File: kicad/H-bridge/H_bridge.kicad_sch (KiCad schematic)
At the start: 34 parts, among them J1 Screw_Terminal_01x02, J2 Conn_Coaxial, J3 Loop_terminals, J4 Coil_terminals, Q1 IAUT300N10S5N014ATMA1, Q2 IAUT300N10S5N014ATMA1, Q3 IAUT300N10S5N014ATMA1, Q4 IAUT300N10S5N014ATMA1, U1 LTV-817, U2 PDS1-S15-S15-M, U3 HIP4080A

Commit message: First iteration of the layout
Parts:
- removed C8: C, symbol Device:C
- removed J3: Loop_terminals, symbol Connector:Screw_Terminal_01x02
- removed J4: Coil_terminals, symbol Connector:Screw_Terminal_01x02
- removed R7: R_US, symbol Device:R_US
- added J3: 2453710000, footprints:CONN_2453710000, symbol Connector:Screw_Terminal_01x04
- added RV1: V20E50P (80V), Varistor:RV_Disc_D15.5mm_W7.5mm_P7.5mm, symbol Device:Varistor_US
- C1, C2, C5, C6: footprint Capacitors_SMD:C_0805 -> Capacitor_SMD:C_0805_2012Metric
- C3, C4, C7, C9: footprint (none) -> Capacitor_SMD:C_0805_2012Metric
- D1, D2: value D -> PMEG10020AELRX; footprint (none) -> Diode_SMD:Nexperia_CFP3_SOD-123W; DIGIKEY (none) -> 1727-2283-1-ND; PARTNO (none) -> PMEG10020AELRX
- Q1, Q2, Q3, Q4: footprint (none) -> Package_TO_SOT_SMD:Infineon_PG-HSOF-8-1_ThermalVias
- R2: footprint Resistors_SMD:R_0805 -> Resistor_SMD:R_0805_2012Metric
- R3, R4, R5, R6: footprint (none) -> Resistor_SMD:R_0805_2012Metric
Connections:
- net GNDD: now also J3.4 (Pin_4), RV1.2
- net at R2.1, U1.3: now also U3.6 (IN+)
- net Coil_B: now reaches C3.2, Q3.3 (S), Q4.1 (D), U3.12 (AHS)
- net Coil_B: now also J3.3 (Pin_3)
- net Coil_A: now reaches C7.2, Q1.3 (S), Q2.1 (D), U3.19 (BHS)
- net Coil_A: now also J3.2 (Pin_2)
- net Current_in: now reaches Q1.1 (D), Q3.1 (D)
- net Current_in: now also J3.1 (Pin_1), RV1.1
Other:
- moved on the sheet: R2

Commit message: 2nd iteration
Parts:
- added H1, H2, H3, H4: MountingHole, MountingHole:MountingHole_3.5mm, symbol Mechanical:MountingHole
- Q1, Q2, Q3, Q4: symbol Simulation_SPICE:NMOS -> Device:Q_NMOS_GDS
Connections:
- net Coil_A: now also Q2.2 (D); no longer Q2.1 (D)
- net Coil_B: now also Q4.2 (D); no longer Q4.1 (D)
- net Current_in: now also Q1.2 (D), Q3.2 (D); no longer Q1.1 (D), Q3.1 (D)
- net at U3.13 (ALO): now also Q4.1 (G); no longer Q4.2 (G)
- net at U3.11 (AHO): now also Q3.1 (G); no longer Q3.2 (G)
- net at U3.20 (BHO): now also Q1.1 (G); no longer Q1.2 (G)
- net at U3.18 (BLO): now also Q2.1 (G); no longer Q2.2 (G)

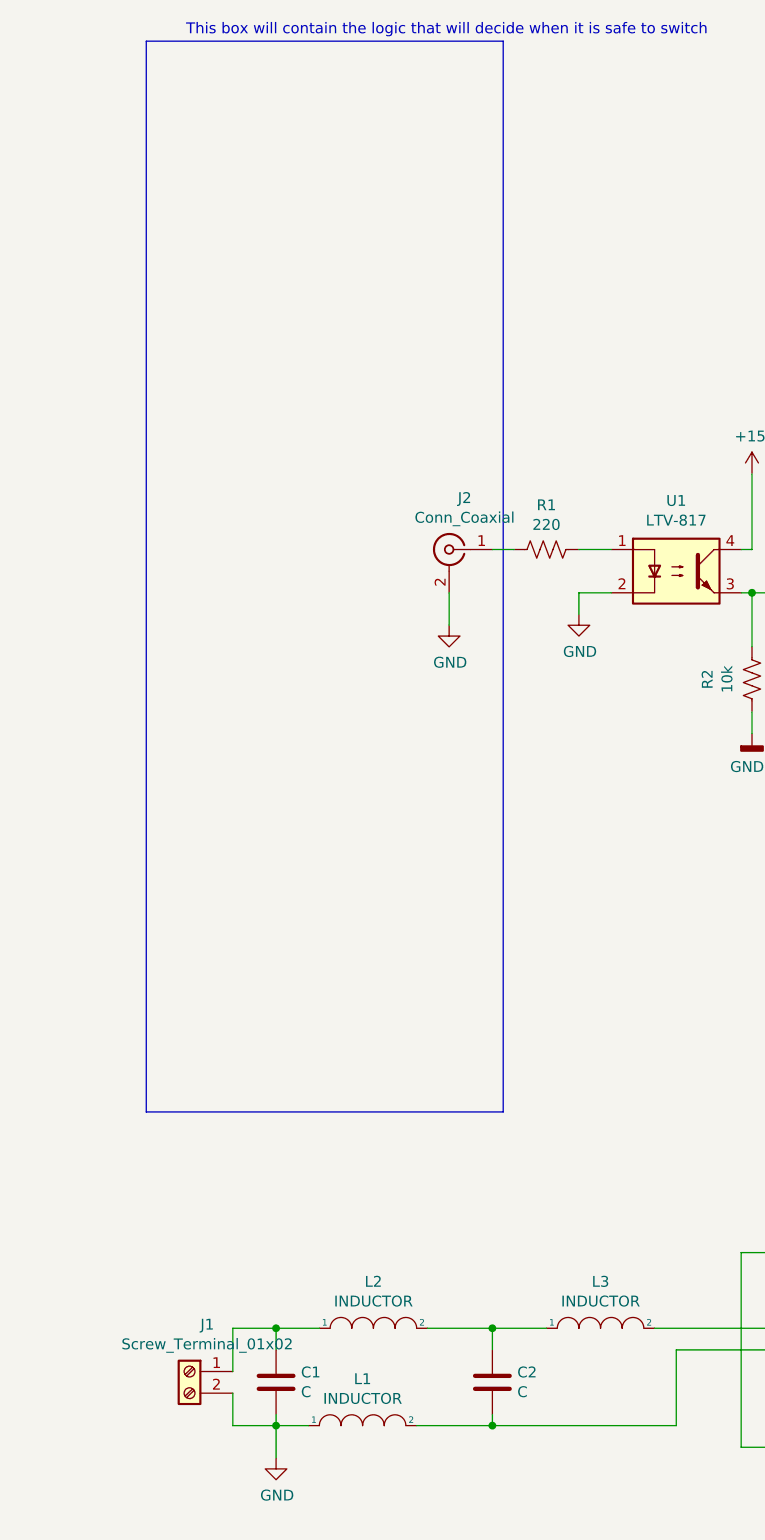
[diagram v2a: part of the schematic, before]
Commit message: H_bridge circuit with current control ciruit added
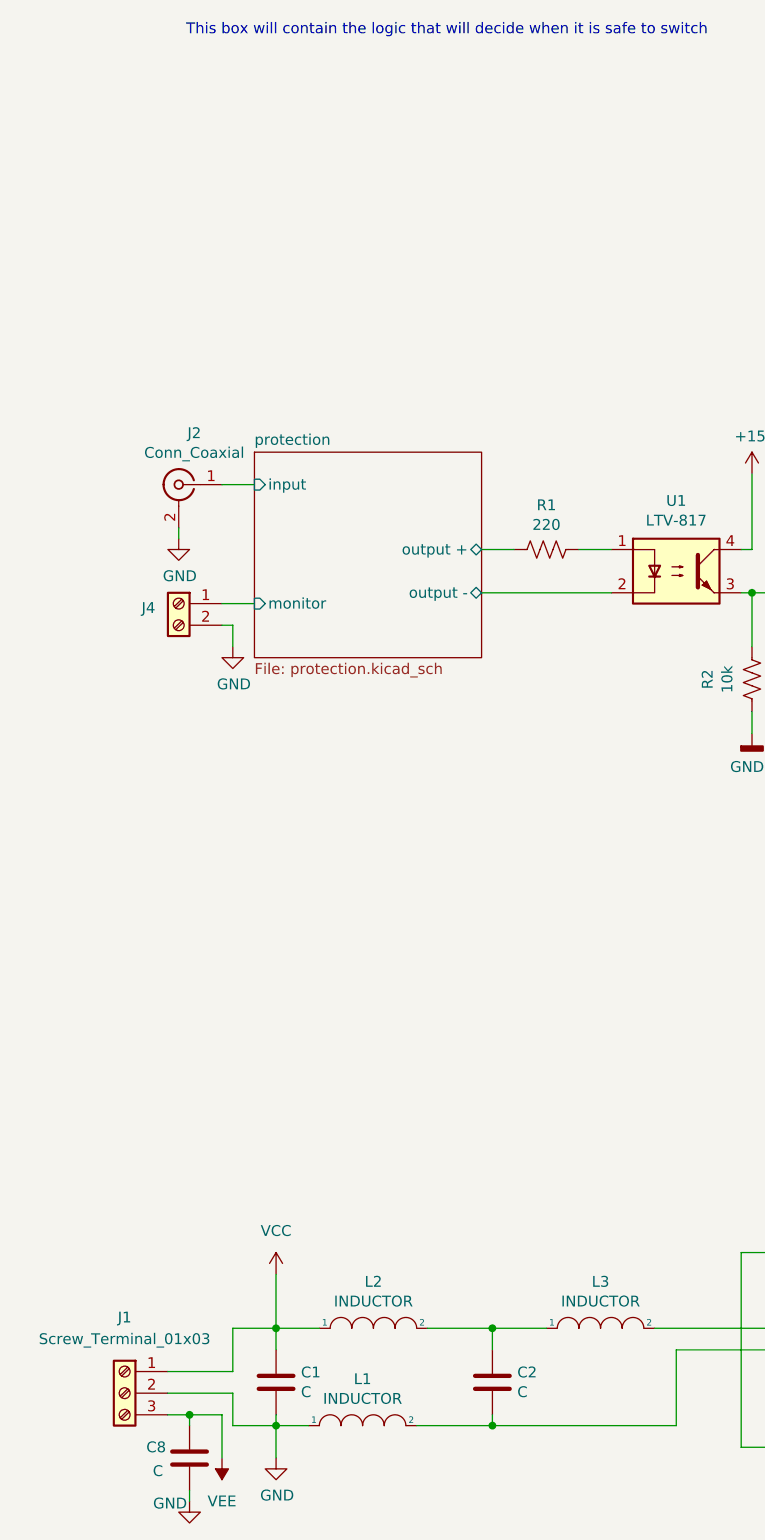
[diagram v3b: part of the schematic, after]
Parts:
- removed J1: Screw_Terminal_01x02, TerminalBlock_4UCON:TerminalBlock_4UCON_19963_02x3.5mm_Straight, symbol Connector:Screw_Terminal_01x02
- added BOM1: ~, symbol Connecteor:spare
- added C8: C, Capacitor_SMD:C_0805_2012Metric, symbol Device:C
- added J1: Screw_Terminal_01x03, TerminalBlock_4Ucon:TerminalBlock_4Ucon_1x03_P3.50mm_Horizontal, symbol Connector:Screw_Terminal_01x03
- added J4: Screw_Terminal_01x02, TerminalBlock_4Ucon:TerminalBlock_4Ucon_1x02_P3.50mm_Horizontal, symbol Connector:Screw_Terminal_01x02
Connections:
- net GND: now also C8.2, J1.2 (Pin_2), J4.2 (Pin_2); no longer U1.2
- net protection/input: now reaches J2.1 (In)
- net protection/input: no longer R1.2
- net VCC: now reaches C1.1, L2.1
- net VCC: now also J1.1 (Pin_1)
- new net VEE: C8.1, J1.3 (Pin_3)
- new net protection/monitor: J4.1 (Pin_1)
- new net protection/output +: R1.2
- new net protection/output -: U1.2
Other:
- added sheet protection (protection.kicad_sch)
- moved on the sheet: J2

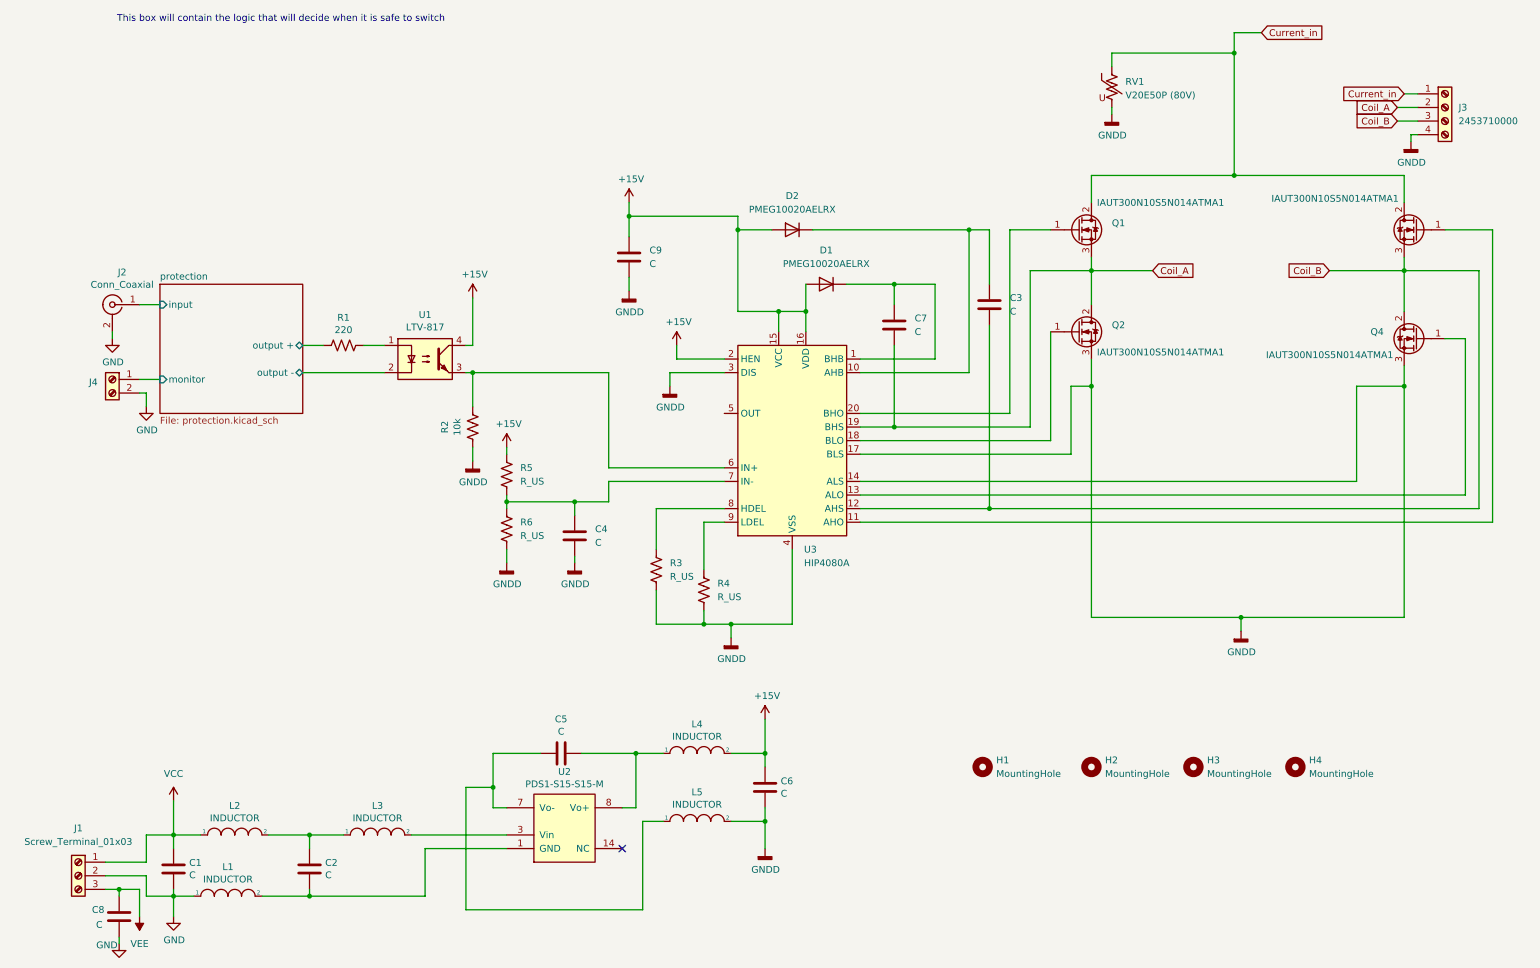
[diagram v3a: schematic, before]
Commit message: Added C18, logo and other footprints
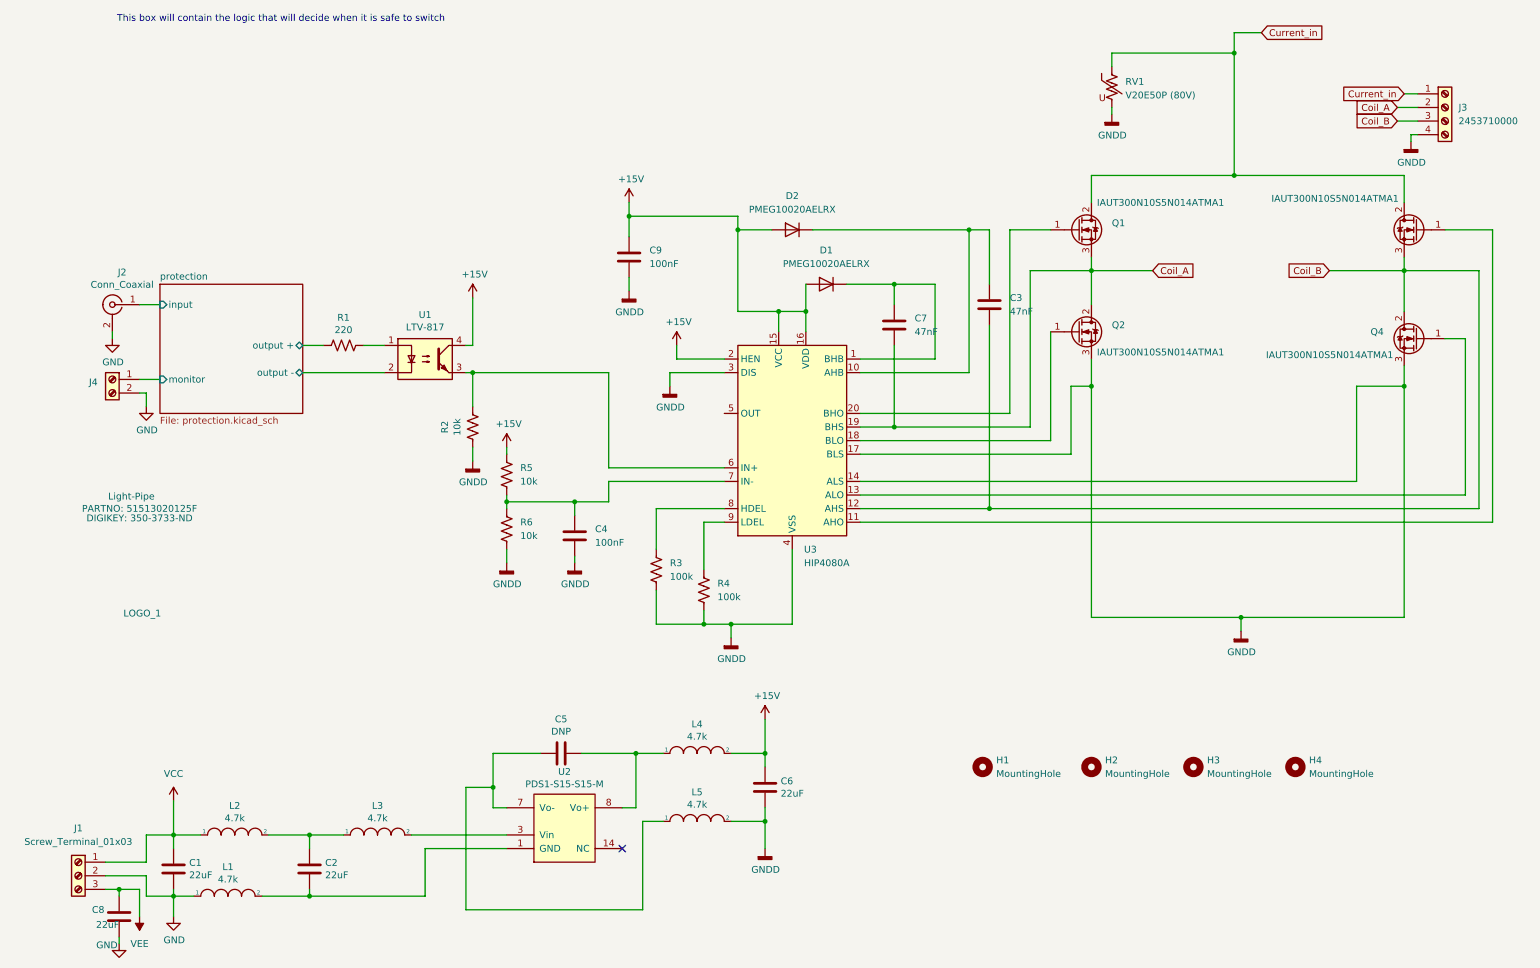
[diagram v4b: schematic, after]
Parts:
- added LOGO_1: ~, footprints:JQI-Logo, symbol Connecteor:spare
- BOM1: value ~ -> Light-Pipe; DIGIKEY (none) -> 350-3733-ND; PARTNO (none) -> 51513020125F
- C1, C2, C6, C8: value C -> 22uF; DIGIKEY (none) -> 445-14428-1-ND; PARTNO (none) -> C2012X5R1V226M125AC
- C3, C7: value C -> 47nF; DIGIKEY (none) -> 399-C0805C473K2RECAUTOCT-ND; PARTNO (none) -> C0805C473K2RECAUTO
- C4, C9: value C -> 100nF; DIGIKEY (none) -> 311-1140-1-ND; PARTNO (none) -> CC0805KRX7R9BB104
- C5: value C -> DNP
- J2: DIGIKEY (none) -> A32260-ND; PARTNO (none) -> 5227161-7
- L1, L2, L3, L4, L5: value INDUCTOR -> 4.7k; DIGIKEY (none) -> 490-BLM21HE472SN1LCT-ND; PARTNO (none) -> BLM21HE472SN1L
- R1: DIGIKEY (none) -> A129741CT-ND; PARTNO (none) -> CRGCQ0805F220R
- R2: DIGIKEY (none) -> A129761CT-ND; PARTNO (none) -> CRGCQ0805F10K
- R3, R4: value R_US -> 100k; DIGIKEY (none) -> A106052CT-ND; PARTNO (none) -> CRG0805F100K
- R5, R6: value R_US -> 10k; DIGIKEY (none) -> A129761CT-ND; PARTNO (none) -> CRGCQ0805F10K
- U1: DIGIKEY (none) -> 160-1366-5-ND; PARTNO (none) -> LTV-817
- U2: DIGIKEY (none) -> 102-4546-ND; PARTNO (none) -> PDS1-S15-S15-M
